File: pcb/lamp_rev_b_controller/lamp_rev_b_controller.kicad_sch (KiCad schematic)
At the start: 155 parts, among them J1 TYPE-C 3.1 MT 16P, J10 2-pin NTC header, J11 2-pin NTC header, J12 DB128H-5.08-2P-BK-S, J13 DB128H-5.08-2P-BK-S, J15 DB128H-5.08-2P-BK-S, J16 LED NTC/ID header, J17 External camera sync header, J18 SPI/FIFO camera module header, J19 Lid/cartridge/cutoff interloc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, J2 DB128H-5.08-2P-BK-S, J20 Fan PWM/tach header, J21 2x3 UART/programming header, J22 I2C expansion header, J23 Analog optical diagnostic hea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, J24 DB128H-5.08-2P high-current h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, J4 2-pin NTC header, J5 2-pin NTC header, J6 2-pin NTC header, J7 2-pin NTC header, J8 2-pin NTC header, J9 2-pin NTC header, Q1 IRLB3813PBF TO-220 12V protot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, Q2 IRLB3813PBF TO-220 12V protot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, U1 ESP32-S3-WROOM-1-N16, U10 INA180A1IDBVR gain 20 LED cur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, U2 USBLC6-2SC6, U3 Diodes AP63203WU-7 fixed 3.3V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, U4 ADS1115IDGSR, U5 CD74HC4051M, U6 TC4427ACOA/TC4427EPA, U7 CUI/Bel P7805-2000-S 5V 2A 8-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, U8 Mean Well LDD-700H 700mA CC b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, U9 SN74LVC1G08DBVR LED_EXC_PWM A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

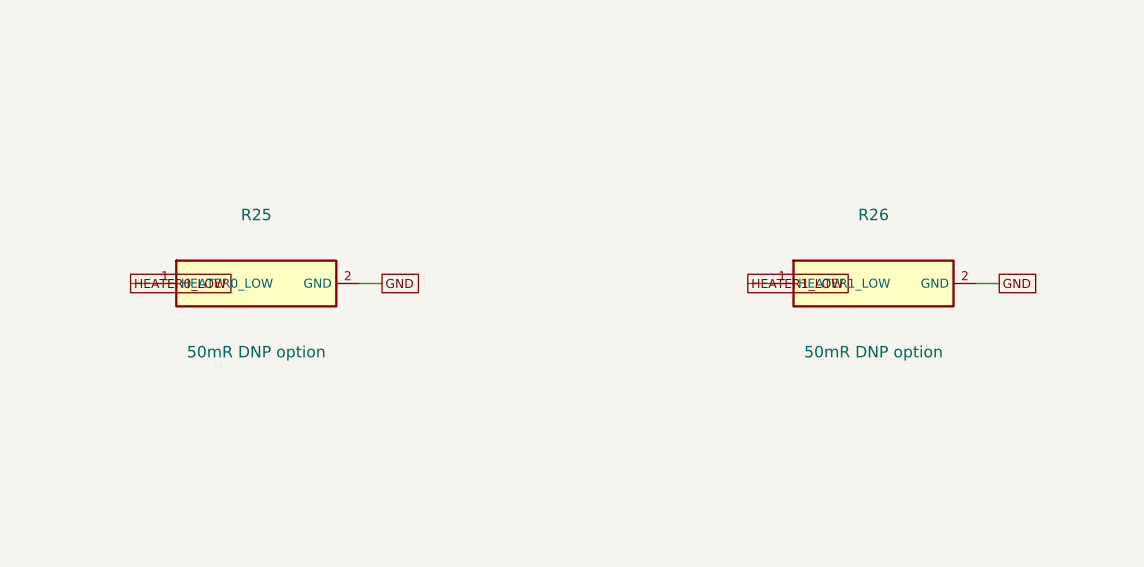
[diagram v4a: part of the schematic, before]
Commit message: Reconcile Rev B BOM and CPL fabrication classes
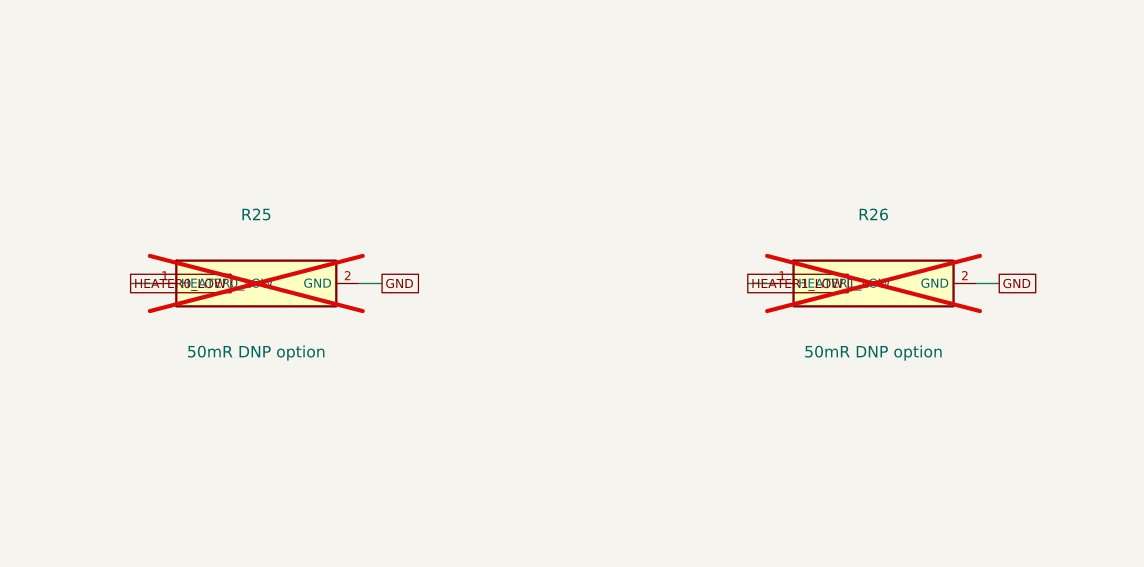
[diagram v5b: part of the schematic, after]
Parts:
- R25, R26: now not fitted
- TP_3V3, TP_3V3A, TP_5V, TP_ADS_AIN0, TP_ADS_AIN1, TP_ADS_AIN2, TP_ADS_AIN3, TP_AUX_ANALOG, TP_BOOT, TP_CAM_CS, TP_CAM_FRAME, TP_CAM_PWDN, TP_CAM_RESET, TP_CART, TP_CUTOFF, TP_EN, TP_EXPOSURE, TP_FAN_PWM, TP_FAN_TACH, TP_FAULT, TP_FRAME_TRIG, TP_GND, TP_HEATER0_GATE, TP_HEATER0_LOW, TP_HEATER0_PWM, TP_HEATER1_GATE, TP_HEATER1_LOW, TP_HEATER1_PWM, TP_HEATER_ARM, TP_HEATER_SENSE, TP_I2C_SCL, TP_I2C_SDA, TP_LATCH, TP_LED_EN, TP_LED_PWM, TP_LED_SENSE, TP_LED_SUPPLY, TP_LED_SYNC, TP_LID, TP_RUN, TP_SD_CS, TP_SPARE42, TP_SPI_MISO, TP_SPI_MOSI, TP_SPI_SCLK, TP_THERM_EN, TP_THERM_OUT, TP_THERM_S0, TP_THERM_S1, TP_THERM_S2, TP_UART_RX, TP_UART_TX, TP_USB_CC1, TP_USB_CC2, TP_USB_DN, TP_USB_DP, TP_VBUS, TP_VDRV, TP_VIN, TP_VIN_HEATER, TP_VIN_PROT: LCSC Part DNP_TESTPOINT -> VIRTUAL_TESTPOINT; Notes Schematic capture test point generated from placement.toml -> Virtual PCB test pad generated from placement.toml; exclude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; now left out of the parts list

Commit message: Resolve Rev B controller U1 exposed pad grounding
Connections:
- net GND_EP is gone; now on net GND: U1.41 (GND)
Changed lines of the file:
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@@
     (stroke (width 0) (type default))
   )
-  (global_label "GND_EP" (shape passive)
+  (global_label "GND" (shape passive)
     (at 113.03 746.76 0)
     (effects (font (size 1.0 1.0)) (justify left))

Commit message: Complete Rev B analog front end reconciliation
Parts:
- removed U10: INA180A1IDBVR gain 20 LED current sense, lcsc:SOT-23-5, symbol LF_CAPTURE_U10
- removed U9: SN74LVC1G08DBVR LED_EXC_PWM AND LED_EXC_EN, lcsc:SOT-23-5, symbol LF_CAPTURE_U9
- J23: Notes Analog optical diagnostic header. -> Analog optical diagnostic header. Pins 3 and 4 are the same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
- R25: value 50mR DNP option -> 50mR DNP forbidden low-side bypass placeholder; Notes HEATER0 optional current shunt. -> DNP forbidden bypass placeholder. Populating R25 directly b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
- R26: value 50mR DNP option -> 50mR DNP forbidden low-side bypass placeholder; Notes HEATER1 optional current shunt. -> DNP forbidden bypass placeholder. Populating R26 directly b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
- TP_ADS_AIN0: value test point ADS_AIN0 -> test point THERM_MUX_OUT
- TP_ADS_AIN2: renamed from TP_ADS_AIN1; value test point ADS_AIN1 -> test point LED_CURRENT_SENSE; symbol LF_CAPTURE_TP_ADS_AIN1 -> LF_CAPTURE_TP_ADS_AIN2
- TP_ADS_AIN3: renamed from TP_ADS_AIN2; value test point ADS_AIN2 -> test point AUX_ANALOG_IN; symbol LF_CAPTURE_TP_ADS_AIN2 -> LF_CAPTURE_TP_ADS_AIN3
- TP_AUX_ANALOG: renamed from TP_ADS_AIN3; value test point ADS_AIN3 -> test point AUX_ANALOG_IN; symbol LF_CAPTURE_TP_ADS_AIN3 -> LF_CAPTURE_TP_AUX_ANALOG
- TP_BOOT: renamed from TP_AUX_ANALOG; value test point AUX_ANALOG_IN -> test point ESP_GPIO0_BOOT; symbol LF_CAPTURE_TP_AUX_ANALOG -> LF_CAPTURE_TP_BOOT
- TP_CAM_CS: renamed from TP_BOOT; value test point ESP_GPIO0_BOOT -> test point CAM_CS_N; symbol LF_CAPTURE_TP_BOOT -> LF_CAPTURE_TP_CAM_CS
- TP_CAM_FRAME: renamed from TP_CAM_CS; value test point CAM_CS_N -> test point CAM_FRAME_INT; symbol LF_CAPTURE_TP_CAM_CS -> LF_CAPTURE_TP_CAM_FRAME
- TP_CAM_PWDN: renamed from TP_CAM_FRAME; value test point CAM_FRAME_INT -> test point CAM_PWDN_N; symbol LF_CAPTURE_TP_CAM_FRAME -> LF_CAPTURE_TP_CAM_PWDN
- TP_CAM_RESET: renamed from TP_CAM_PWDN; value test point CAM_PWDN_N -> test point CAM_RESET_N; symbol LF_CAPTURE_TP_CAM_PWDN -> LF_CAPTURE_TP_CAM_RESET
- TP_CART: renamed from TP_CAM_RESET; value test point CAM_RESET_N -> test point CART_PRESENT_N; symbol LF_CAPTURE_TP_CAM_RESET -> LF_CAPTURE_TP_CART
- TP_CUTOFF: renamed from TP_CART; value test point CART_PRESENT_N -> test point AUX_IO0_THERMAL_CUTOFF_OK; symbol LF_CAPTURE_TP_CART -> LF_CAPTURE_TP_CUTOFF
- TP_EN: renamed from TP_CUTOFF; value test point AUX_IO0_THERMAL_CUTOFF_OK -> test point ESP_EN; symbol LF_CAPTURE_TP_CUTOFF -> LF_CAPTURE_TP_EN
- TP_EXPOSURE: renamed from TP_EN; value test point ESP_EN -> test point EXPOSURE_ACTIVE_IN; symbol LF_CAPTURE_TP_EN -> LF_CAPTURE_TP_EXPOSURE
- TP_FAN_PWM: renamed from TP_EXPOSURE; value test point EXPOSURE_ACTIVE_IN -> test point FAN_PWM; symbol LF_CAPTURE_TP_EXPOSURE -> LF_CAPTURE_TP_FAN_PWM
- TP_FAN_TACH: renamed from TP_FAN_PWM; value test point FAN_PWM -> test point FAN_TACH; symbol LF_CAPTURE_TP_FAN_PWM -> LF_CAPTURE_TP_FAN_TACH
- TP_FAULT: renamed from TP_FAN_TACH; value test point FAN_TACH -> test point STATUS_FAULT_LED; symbol LF_CAPTURE_TP_FAN_TACH -> LF_CAPTURE_TP_FAULT
- TP_FRAME_TRIG: renamed from TP_FAULT; value test point STATUS_FAULT_LED -> test point FRAME_TRIG_OUT; symbol LF_CAPTURE_TP_FAULT -> LF_CAPTURE_TP_FRAME_TRIG
- TP_GND: renamed from TP_FRAME_TRIG; value test point FRAME_TRIG_OUT -> test point GND; symbol LF_CAPTURE_TP_FRAME_TRIG -> LF_CAPTURE_TP_GND
- TP_HEATER0_GATE: renamed from TP_GND; value test point GND -> test point HEATER0_GATE; symbol LF_CAPTURE_TP_GND -> LF_CAPTURE_TP_HEATER0_GATE
- TP_HEATER0_LOW: renamed from TP_HEATER0_GATE; value test point HEATER0_GATE -> test point HEATER0_LOW; symbol LF_CAPTURE_TP_HEATER0_GATE -> LF_CAPTURE_TP_HEATER0_LOW
- TP_HEATER0_PWM: renamed from TP_HEATER0_LOW; value test point HEATER0_LOW -> test point HEATER0_PWM; symbol LF_CAPTURE_TP_HEATER0_LOW -> LF_CAPTURE_TP_HEATER0_PWM
- TP_HEATER1_GATE: renamed from TP_HEATER0_PWM; value test point HEATER0_PWM -> test point HEATER1_GATE; symbol LF_CAPTURE_TP_HEATER0_PWM -> LF_CAPTURE_TP_HEATER1_GATE
- TP_HEATER1_LOW: renamed from TP_HEATER1_GATE; value test point HEATER1_GATE -> test point HEATER1_LOW; symbol LF_CAPTURE_TP_HEATER1_GATE -> LF_CAPTURE_TP_HEATER1_LOW
- TP_HEATER1_PWM: renamed from TP_HEATER1_LOW; value test point HEATER1_LOW -> test point HEATER1_PWM; symbol LF_CAPTURE_TP_HEATER1_LOW -> LF_CAPTURE_TP_HEATER1_PWM
- TP_HEATER_ARM: renamed from TP_HEATER1_PWM; value test point HEATER1_PWM -> test point HEATER_ARM; symbol LF_CAPTURE_TP_HEATER1_PWM -> LF_CAPTURE_TP_HEATER_ARM
- TP_I2C_SCL: renamed from TP_HEATER_ARM; value test point HEATER_ARM -> test point I2C_SCL; symbol LF_CAPTURE_TP_HEATER_ARM -> LF_CAPTURE_TP_I2C_SCL
- TP_I2C_SDA: renamed from TP_HEATER_SENSE; value test point HEATER_SUPPLY_SENSE -> test point I2C_SDA; symbol LF_CAPTURE_TP_HEATER_SENSE -> LF_CAPTURE_TP_I2C_SDA
- TP_LATCH: renamed from TP_I2C_SCL; value test point I2C_SCL -> test point LATCH_LOCKED_N; symbol LF_CAPTURE_TP_I2C_SCL -> LF_CAPTURE_TP_LATCH
- TP_LED_EN: renamed from TP_I2C_SDA; value test point I2C_SDA -> test point LED_EXC_EN; symbol LF_CAPTURE_TP_I2C_SDA -> LF_CAPTURE_TP_LED_EN
- TP_LED_PWM: renamed from TP_LATCH; value test point LATCH_LOCKED_N -> test point LED_EXC_PWM; symbol LF_CAPTURE_TP_LATCH -> LF_CAPTURE_TP_LED_PWM
- TP_LED_SENSE: renamed from TP_LED_EN; value test point LED_EXC_EN -> test point LED_CURRENT_SENSE; symbol LF_CAPTURE_TP_LED_EN -> LF_CAPTURE_TP_LED_SENSE
- TP_LED_SUPPLY: renamed from TP_LED_PWM; value test point LED_EXC_PWM -> test point LED_SUPPLY; symbol LF_CAPTURE_TP_LED_PWM -> LF_CAPTURE_TP_LED_SUPPLY
- TP_LED_SYNC: renamed from TP_LED_SENSE; value test point LED_CURRENT_SENSE -> test point LED_SYNC_OUT; symbol LF_CAPTURE_TP_LED_SENSE -> LF_CAPTURE_TP_LED_SYNC
- TP_LID: renamed from TP_LED_SUPPLY; value test point LED_SUPPLY -> test point LID_CLOSED_N; symbol LF_CAPTURE_TP_LED_SUPPLY -> LF_CAPTURE_TP_LID
- TP_RUN: renamed from TP_LED_SYNC; value test point LED_SYNC_OUT -> test point STATUS_RUN_LED; symbol LF_CAPTURE_TP_LED_SYNC -> LF_CAPTURE_TP_RUN
- TP_SD_CS: renamed from TP_LID; value test point LID_CLOSED_N -> test point SD_CS_N; symbol LF_CAPTURE_TP_LID -> LF_CAPTURE_TP_SD_CS
- TP_SPARE42: renamed from TP_RUN; value test point STATUS_RUN_LED -> test point SPARE_GPIO42; symbol LF_CAPTURE_TP_RUN -> LF_CAPTURE_TP_SPARE42
- TP_SPI_MISO: renamed from TP_SD_CS; value test point SD_CS_N -> test point SPI_MISO; symbol LF_CAPTURE_TP_SD_CS -> LF_CAPTURE_TP_SPI_MISO
- TP_SPI_MOSI: renamed from TP_SPARE42; value test point SPARE_GPIO42 -> test point SPI_MOSI; symbol LF_CAPTURE_TP_SPARE42 -> LF_CAPTURE_TP_SPI_MOSI
- TP_SPI_SCLK: renamed from TP_SPI_MISO; value test point SPI_MISO -> test point SPI_SCLK; symbol LF_CAPTURE_TP_SPI_MISO -> LF_CAPTURE_TP_SPI_SCLK
- TP_THERM_EN: renamed from TP_SPI_MOSI; value test point SPI_MOSI -> test point THERM_MUX_EN_N; symbol LF_CAPTURE_TP_SPI_MOSI -> LF_CAPTURE_TP_THERM_EN
- TP_THERM_OUT: renamed from TP_SPI_SCLK; value test point SPI_SCLK -> test point THERM_MUX_OUT; symbol LF_CAPTURE_TP_SPI_SCLK -> LF_CAPTURE_TP_THERM_OUT
- TP_THERM_S0: renamed from TP_THERM_EN; value test point THERM_MUX_EN_N -> test point THERM_MUX_S0; symbol LF_CAPTURE_TP_THERM_EN -> LF_CAPTURE_TP_THERM_S0
- TP_THERM_S1: renamed from TP_THERM_OUT; value test point THERM_MUX_OUT -> test point THERM_MUX_S1; symbol LF_CAPTURE_TP_THERM_OUT -> LF_CAPTURE_TP_THERM_S1
- TP_THERM_S2: renamed from TP_THERM_S0; value test point THERM_MUX_S0 -> test point THERM_MUX_S2; symbol LF_CAPTURE_TP_THERM_S0 -> LF_CAPTURE_TP_THERM_S2
- TP_UART_RX: renamed from TP_THERM_S1; value test point THERM_MUX_S1 -> test point UART0_RXD; symbol LF_CAPTURE_TP_THERM_S1 -> LF_CAPTURE_TP_UART_RX
- TP_UART_TX: renamed from TP_THERM_S2; value test point THERM_MUX_S2 -> test point UART0_TXD; symbol LF_CAPTURE_TP_THERM_S2 -> LF_CAPTURE_TP_UART_TX
- TP_USB_CC1: renamed from TP_UART_RX; value test point UART0_RXD -> test point USB_CC1; symbol LF_CAPTURE_TP_UART_RX -> LF_CAPTURE_TP_USB_CC1
- TP_USB_CC2: renamed from TP_UART_TX; value test point UART0_TXD -> test point USB_CC2; symbol LF_CAPTURE_TP_UART_TX -> LF_CAPTURE_TP_USB_CC2
- TP_USB_DN: renamed from TP_USB_CC1; value test point USB_CC1 -> test point USB_DN; symbol LF_CAPTURE_TP_USB_CC1 -> LF_CAPTURE_TP_USB_DN
- TP_USB_DP: renamed from TP_USB_CC2; value test point USB_CC2 -> test point USB_DP; symbol LF_CAPTURE_TP_USB_CC2 -> LF_CAPTURE_TP_USB_DP
- TP_VBUS: renamed from TP_USB_DN; value test point USB_DN -> test point VBUS; symbol LF_CAPTURE_TP_USB_DN -> LF_CAPTURE_TP_VBUS
- TP_VDRV: renamed from TP_USB_DP; value test point USB_DP -> test point VDRV; symbol LF_CAPTURE_TP_USB_DP -> LF_CAPTURE_TP_VDRV
- TP_VIN: renamed from TP_VBUS; value test point VBUS -> test point VIN_12_24; symbol LF_CAPTURE_TP_VBUS -> LF_CAPTURE_TP_VIN
- TP_VIN_HEATER: renamed from TP_VDRV; value test point VDRV -> test point VIN_HEATER; symbol LF_CAPTURE_TP_VDRV -> LF_CAPTURE_TP_VIN_HEATER
- TP_VIN_PROT: renamed from TP_VIN; value test point VIN_12_24 -> test point VIN_PROTECTED; symbol LF_CAPTURE_TP_VIN -> LF_CAPTURE_TP_VIN_PROT
- U1: renamed from TP_VIN_HEATER; value test point VIN_HEATER -> ESP32-S3-WROOM-1-N16; footprint lcsc:TESTPOINT_SMD_1.5MM -> lcsc:WIFIM-SMD_ESP32-S3-WROOM-1-N8; symbol LF_CAPTURE_TP_VIN_HEATER -> LF_CAPTURE_U1; LCSC Part VIRTUAL_TESTPOINT -> DigiKey 1965-ESP32-S3-WROOM-1-N16-ND; Notes Virtual PCB test pad generated from placement.toml; exclude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 -> ESP32-S3-WROOM-1-N16 using verified-compatible N8 land patt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; now in the parts list
- U10: renamed from U8; value Mean Well LDD-700H 700mA CC buck LED driver; LDD-1000H C17529736 DNP thermal-validation alternate -> INA180A1IDBVR gain 20 LED current sense; footprint lcsc:MEANWELL_LDD-300-1000H_THT -> lcsc:SOT-23-5; symbol LF_CAPTURE_U8 -> LF_CAPTURE_U10; LCSC Part C17537709 -> C122228; Notes Mean Well LDD-700H LED driver module. LDD-H -Vin/GND and -V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 -> INA180A1IDBVR LED current telemetry across high-side output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
- U2: renamed from TP_VIN_PROT; value test point VIN_PROTECTED -> USBLC6-2SC6; footprint lcsc:TESTPOINT_SMD_1.5MM -> lcsc:SOT-23-6; symbol LF_CAPTURE_TP_VIN_PROT -> LF_CAPTURE_U2; LCSC Part VIRTUAL_TESTPOINT -> C7519; Notes Virtual PCB test pad generated from placement.toml; exclude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 -> USB data ESD protection.; now in the parts list
- U3: renamed from U1; value ESP32-S3-WROOM-1-N16 -> Diodes AP63203WU-7 fixed 3.3V 2A buck; footprint lcsc:WIFIM-SMD_ESP32-S3-WROOM-1-N8 -> lcsc:TSOT26_AP63203WU; symbol LF_CAPTURE_U1 -> LF_CAPTURE_U3; LCSC Part DigiKey 1965-ESP32-S3-WROOM-1-N16-ND -> C780769; Notes ESP32-S3-WROOM-1-N16 using verified-compatible N8 land patt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 -> Diodes AP63203WU-7 fixed 3.3 V buck regulator.
- U4: renamed from U2; value USBLC6-2SC6 -> ADS1115IDGSR; footprint lcsc:SOT-23-6 -> lcsc:MSOP-10_L3.0-W3.0-P0.50-LS5.0-BL; symbol LF_CAPTURE_U2 -> LF_CAPTURE_U4; LCSC Part C7519 -> C37593; Notes USB data ESD protection. -> ADS1115 direct single-ended front end: AIN0 receives the fi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
- U5: renamed from U3; value Diodes AP63203WU-7 fixed 3.3V 2A buck -> CD74HC4051M; footprint lcsc:TSOT26_AP63203WU -> lcsc:SOIC-16_L9.9-W3.9-P1.27-LS6.0-BL; symbol LF_CAPTURE_U3 -> LF_CAPTURE_U5; LCSC Part C780769 -> C139301; Notes Diodes AP63203WU-7 fixed 3.3 V buck regulator. -> CD74HC4051 thermistor mux.
- U6: renamed from U4; value ADS1115IDGSR -> TC4427ACOA/TC4427EPA; footprint lcsc:MSOP-10_L3.0-W3.0-P0.50-LS5.0-BL -> lcsc:SOIC-8_L4.9-W3.9-P1.27-LS6.0-BL; symbol LF_CAPTURE_U4 -> LF_CAPTURE_U6; LCSC Part C37593 -> DigiKey TC4427EPA-ND or C636886 SMD alternate; Notes ADS1115 thermal/slow analog ADC. -> TC4427 dual heater gate-driver interface.
- U7: renamed from U5; value CD74HC4051M -> CUI/Bel P7805-2000-S 5V 2A 8-36V buck module; hand-place no-substitution; footprint lcsc:SOIC-16_L9.9-W3.9-P1.27-LS6.0-BL -> lcsc:P78-2000-S_SIP3; symbol LF_CAPTURE_U5 -> LF_CAPTURE_U7; LCSC Part C139301 -> C2848816; Notes CD74HC4051 thermistor mux. -> CUI/Bel P7805-2000-S 5 V / 2 A buck module.
- U8: renamed from U6; value TC4427ACOA/TC4427EPA -> Mean Well LDD-700H 700mA CC buck LED driver; LDD-1000H C17529736 DNP thermal-validation alternate; footprint lcsc:SOIC-8_L4.9-W3.9-P1.27-LS6.0-BL -> lcsc:MEANWELL_LDD-300-1000H_THT; symbol LF_CAPTURE_U6 -> LF_CAPTURE_U8; LCSC Part DigiKey TC4427EPA-ND or C636886 SMD alternate -> C17537709; Notes TC4427 dual heater gate-driver interface. -> Mean Well LDD-700H LED driver module. LDD-H -Vin/GND and -V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
- U9: renamed from U7; value CUI/Bel P7805-2000-S 5V 2A 8-36V buck module; hand-place no-substitution -> SN74LVC1G08DBVR LED_EXC_PWM AND LED_EXC_EN; footprint lcsc:P78-2000-S_SIP3 -> lcsc:SOT-23-5; symbol LF_CAPTURE_U7 -> LF_CAPTURE_U9; LCSC Part C2848816 -> C7666; Notes CUI/Bel P7805-2000-S 5 V / 2 A buck module. -> SN74LVC1G08DBVR gates LED_EXC_PWM and LED_EXC_EN.
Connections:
- net HEATER_SUPPLY_SENSE is gone; now on net I2C_SDA: TP_I2C_SDA.1 (I2C_SDA)
- net +3V3: now also U1.2 (+3V3), U10.5 (+3V3), U3.1 (+3V3), U4.8 (+3V3), U9.5 (+3V3); no longer U3.2 (+3V3), U5.1 (+3V3), U6.8 (+3V3)
- net +3V3_ANA: now also U5.16 (+3V3_ANA); no longer U7.16 (+3V3_ANA)
- net +5V: now also U3.2 (+5V), U3.4 (+5V), U7.3 (+5V); no longer U5.2 (+5V), U5.4 (+5V), U9.3 (+5V)
- net 3V3_BST: now also U3.6 (3V3_BST); no longer U5.6 (3V3_BST)
- net 3V3_SW: now also U3.5 (3V3_SW); no longer U5.5 (3V3_SW)
- net AUX_ANALOG_IN: now also J23.3 (AUX_ANALOG_IN), TP_ADS_AIN3.1 (AUX_ANALOG_IN), TP_AUX_ANALOG.1 (AUX_ANALOG_IN), U4.7 (AUX_ANALOG_IN); no longer TP_BOOT.1 (AUX_ANALOG_IN)
- net AUX_IO0_THERMAL_CUTOFF_OK: now also TP_CUTOFF.1 (AUX_IO0_THERMAL_CUTOFF_OK), U1.32 (AUX_IO0_THERMAL_CUTOFF_OK); no longer TP_EN.1 (AUX_IO0_THERMAL_CUTOFF_OK), U3.32 (AUX_IO0_THERMAL_CUTOFF_OK)
- net CAM_CS_N: now also TP_CAM_CS.1 (CAM_CS_N), U1.20 (CAM_CS_N); no longer TP_CAM_FRAME.1 (CAM_CS_N), U3.20 (CAM_CS_N)
- net CAM_FRAME_INT: now also TP_CAM_FRAME.1 (CAM_FRAME_INT), U1.21 (CAM_FRAME_INT); no longer TP_CAM_PWDN.1 (CAM_FRAME_INT), U3.21 (CAM_FRAME_INT)
- net CAM_PWDN_N: now also TP_CAM_PWDN.1 (CAM_PWDN_N), U1.22 (CAM_PWDN_N); no longer TP_CAM_RESET.1 (CAM_PWDN_N), U3.22 (CAM_PWDN_N)
- net CAM_RESET_N: now also TP_CAM_RESET.1 (CAM_RESET_N), U1.8 (CAM_RESET_N); no longer TP_CART.1 (CAM_RESET_N), U3.8 (CAM_RESET_N)
- net CART_PRESENT_N: now also TP_CART.1 (CART_PRESENT_N), U1.31 (CART_PRESENT_N); no longer TP_CUTOFF.1 (CART_PRESENT_N), U3.31 (CART_PRESENT_N)
- net ESP_EN: now also TP_EN.1 (ESP_EN), U1.3 (ESP_EN); no longer TP_EXPOSURE.1 (ESP_EN), U3.3 (ESP_EN)
- net ESP_GPIO0_BOOT: now also TP_BOOT.1 (ESP_GPIO0_BOOT), U1.27 (ESP_GPIO0_BOOT); no longer TP_CAM_CS.1 (ESP_GPIO0_BOOT), U3.27 (ESP_GPIO0_BOOT)
- net EXPOSURE_ACTIVE_IN: now also TP_EXPOSURE.1 (EXPOSURE_ACTIVE_IN), U1.29 (EXPOSURE_ACTIVE_IN); no longer TP_FAN_PWM.1 (EXPOSURE_ACTIVE_IN), U3.29 (EXPOSURE_ACTIVE_IN)
- net FAN_PWM: now also TP_FAN_PWM.1 (FAN_PWM); no longer TP_FAN_TACH.1 (FAN_PWM)
- net FAN_TACH: now also TP_FAN_TACH.1 (FAN_TACH); no longer TP_FAULT.1 (FAN_TACH)
- net FRAME_TRIG_OUT: now also TP_FRAME_TRIG.1 (FRAME_TRIG_OUT), U1.25 (FRAME_TRIG_OUT); no longer TP_GND.1 (FRAME_TRIG_OUT), U3.25 (FRAME_TRIG_OUT)
- net GND: now also TP_GND.1 (GND), U1.1 (GND), U1.40 (GND), U1.41 (GND), U2.2 (GND), U3.3 (GND), U4.1 (GND), U4.3 (GND), U5.7 (GND), U5.8 (GND), U6.4 (GND), U7.2 (GND), U8.1 (GND), U8.2 (GND); no longer TP_HEATER0_GATE.1 (GND), U10.1 (GND), U3.1 (GND), U3.40 (GND), U3.41 (GND), U4.2 (GND), U5.3 (GND), U6.1 (GND), U7.7 (GND), U7.8 (GND), U8.3 (GND), U8.4 (GND)
- net HEATER0_GATE: now also TP_HEATER0_GATE.1 (HEATER0_GATE), U6.7 (HEATER0_GATE); no longer TP_HEATER0_LOW.1 (HEATER0_GATE), U8.7 (HEATER0_GATE)
- net HEATER0_LOW: now also TP_HEATER0_LOW.1 (HEATER0_LOW); no longer TP_HEATER0_PWM.1 (HEATER0_LOW)
- net HEATER0_PWM: now also TP_HEATER0_PWM.1 (HEATER0_PWM), U1.10 (HEATER0_PWM), U6.2 (HEATER0_PWM); no longer TP_HEATER1_GATE.1 (HEATER0_PWM), U3.10 (HEATER0_PWM), U8.2 (HEATER0_PWM)
- net HEATER1_GATE: now also TP_HEATER1_GATE.1 (HEATER1_GATE), U6.5 (HEATER1_GATE); no longer TP_HEATER1_LOW.1 (HEATER1_GATE), U8.5 (HEATER1_GATE)
- net HEATER1_LOW: now also TP_HEATER1_LOW.1 (HEATER1_LOW); no longer TP_HEATER1_PWM.1 (HEATER1_LOW)
- net HEATER1_PWM: now also TP_HEATER1_PWM.1 (HEATER1_PWM), U1.11 (HEATER1_PWM), U6.8 (HEATER1_PWM); no longer TP_HEATER_ARM.1 (HEATER1_PWM), U3.11 (HEATER1_PWM), U8.8 (HEATER1_PWM)
- net HEATER_ARM: now also TP_HEATER_ARM.1 (HEATER_ARM), U1.9 (HEATER_ARM), U6.1 (HEATER_ARM); no longer TP_I2C_SCL.1 (HEATER_ARM), U3.9 (HEATER_ARM), U8.1 (HEATER_ARM)
- net I2C_SCL: now also TP_I2C_SCL.1 (I2C_SCL), U1.38 (I2C_SCL), U4.10 (I2C_SCL); no longer TP_LATCH.1 (I2C_SCL), U3.38 (I2C_SCL), U6.10 (I2C_SCL)
- net I2C_SDA: now also U1.39 (I2C_SDA), U4.9 (I2C_SDA); no longer TP_LED_EN.1 (I2C_SDA), U3.39 (I2C_SDA), U6.9 (I2C_SDA)
- net LATCH_LOCKED_N: now also TP_LATCH.1 (LATCH_LOCKED_N); no longer TP_LED_PWM.1 (LATCH_LOCKED_N)
- net LED_CURRENT_SENSE: now also TP_ADS_AIN2.1 (LED_CURRENT_SENSE), TP_LED_SENSE.1 (LED_CURRENT_SENSE), U10.4 (LED_CURRENT_SENSE), U4.6 (LED_CURRENT_SENSE); no longer TP_LED_SYNC.1 (LED_CURRENT_SENSE)
- net LED_DIM_DRIVE: now also U8.22 (LED_DIM_DRIVE); no longer U10.22 (LED_DIM_DRIVE)
- net LED_DIM_GATE: now also U9.4 (LED_DIM_GATE)
- net LED_DRV_PLUS: now also U10.1 (LED_DRV_PLUS), U8.13 (LED_DRV_PLUS), U8.14 (LED_DRV_PLUS); no longer U10.13 (LED_DRV_PLUS), U10.14 (LED_DRV_PLUS)
- net LED_EXC_EN: now also TP_LED_EN.1 (LED_EXC_EN), U1.24 (LED_EXC_EN), U9.3 (LED_EXC_EN); no longer TP_LED_SENSE.1 (LED_EXC_EN), U3.24 (LED_EXC_EN)
- net LED_EXC_PWM: now also TP_LED_PWM.1 (LED_EXC_PWM), U1.7 (LED_EXC_PWM), U9.1 (LED_EXC_PWM); no longer TP_LED_SUPPLY.1 (LED_EXC_PWM), U3.7 (LED_EXC_PWM)
- net LED_MINUS: now also U8.11 (LED_MINUS), U8.12 (LED_MINUS); no longer U10.11 (LED_MINUS), U10.12 (LED_MINUS)
- net LED_PLUS: now also U10.3 (LED_PLUS)
- net LED_SUPPLY: now also TP_LED_SUPPLY.1 (LED_SUPPLY), U8.23 (LED_SUPPLY), U8.24 (LED_SUPPLY); no longer TP_LID.1 (LED_SUPPLY), U10.23 (LED_SUPPLY), U10.24 (LED_SUPPLY)
- net LED_SYNC_OUT: now also TP_LED_SYNC.1 (LED_SYNC_OUT), U1.28 (LED_SYNC_OUT); no longer TP_RUN.1 (LED_SYNC_OUT), U3.28 (LED_SYNC_OUT)
- net LID_CLOSED_N: now also TP_LID.1 (LID_CLOSED_N), U1.30 (LID_CLOSED_N); no longer TP_SD_CS.1 (LID_CLOSED_N), U3.30 (LID_CLOSED_N)
- net SD_CS_N: now also TP_SD_CS.1 (SD_CS_N), U1.23 (SD_CS_N); no longer TP_SPI_MISO.1 (SD_CS_N), U3.23 (SD_CS_N)
- net SPARE_GPIO42: now also TP_SPARE42.1 (SPARE_GPIO42), U1.35 (SPARE_GPIO42); no longer TP_SPI_MOSI.1 (SPARE_GPIO42), U3.35 (SPARE_GPIO42)
- net SPI_MISO: now also TP_SPI_MISO.1 (SPI_MISO), U1.19 (SPI_MISO); no longer TP_SPI_SCLK.1 (SPI_MISO), U3.19 (SPI_MISO)
- net SPI_MOSI: now also TP_SPI_MOSI.1 (SPI_MOSI), U1.18 (SPI_MOSI); no longer TP_THERM_EN.1 (SPI_MOSI), U3.18 (SPI_MOSI)
- net SPI_SCLK: now also TP_SPI_SCLK.1 (SPI_SCLK), U1.17 (SPI_SCLK); no longer TP_THERM_OUT.1 (SPI_SCLK), U3.17 (SPI_SCLK)
- net STATUS_FAULT_LED: now also TP_FAULT.1 (STATUS_FAULT_LED), U1.34 (STATUS_FAULT_LED); no longer TP_FRAME_TRIG.1 (STATUS_FAULT_LED), U3.34 (STATUS_FAULT_LED)
- net STATUS_RUN_LED: now also TP_RUN.1 (STATUS_RUN_LED), U1.33 (STATUS_RUN_LED); no longer TP_SPARE42.1 (STATUS_RUN_LED), U3.33 (STATUS_RUN_LED)
- net THERM_CH_0: now also U5.13 (THERM_CH_0); no longer U7.13 (THERM_CH_0)
- net THERM_CH_1: now also U5.14 (THERM_CH_1); no longer U7.14 (THERM_CH_1)
- net THERM_CH_2: now also U5.15 (THERM_CH_2); no longer U7.15 (THERM_CH_2)
- net THERM_CH_3: now also U5.12 (THERM_CH_3); no longer U7.12 (THERM_CH_3)
- net THERM_CH_4: now also U5.1 (THERM_CH_4); no longer U7.1 (THERM_CH_4)
- net THERM_CH_5: now also U5.5 (THERM_CH_5); no longer U7.5 (THERM_CH_5)
- net THERM_CH_6: now also U5.2 (THERM_CH_6); no longer U7.2 (THERM_CH_6)
- net THERM_CH_7: now also U5.4 (THERM_CH_7); no longer U7.4 (THERM_CH_7)
- net THERM_MUX_EN_N: now also TP_THERM_EN.1 (THERM_MUX_EN_N), U1.12 (THERM_MUX_EN_N), U5.6 (THERM_MUX_EN_N); no longer TP_THERM_S0.1 (THERM_MUX_EN_N), U3.12 (THERM_MUX_EN_N), U7.6 (THERM_MUX_EN_N)
- net THERM_MUX_OUT: now also TP_ADS_AIN0.1 (THERM_MUX_OUT), TP_THERM_OUT.1 (THERM_MUX_OUT), U4.4 (THERM_MUX_OUT), U5.3 (THERM_MUX_OUT); no longer TP_THERM_S1.1 (THERM_MUX_OUT), U7.3 (THERM_MUX_OUT)
- net THERM_MUX_S0: now also TP_THERM_S0.1 (THERM_MUX_S0), U1.4 (THERM_MUX_S0), U5.11 (THERM_MUX_S0); no longer TP_THERM_S2.1 (THERM_MUX_S0), U3.4 (THERM_MUX_S0), U7.11 (THERM_MUX_S0)
- net THERM_MUX_S1: now also TP_THERM_S1.1 (THERM_MUX_S1), U1.5 (THERM_MUX_S1), U5.10 (THERM_MUX_S1); no longer TP_UART_RX.1 (THERM_MUX_S1), U3.5 (THERM_MUX_S1), U7.10 (THERM_MUX_S1)
- net THERM_MUX_S2: now also TP_THERM_S2.1 (THERM_MUX_S2), U1.6 (THERM_MUX_S2), U5.9 (THERM_MUX_S2); no longer TP_UART_TX.1 (THERM_MUX_S2), U3.6 (THERM_MUX_S2), U7.9 (THERM_MUX_S2)
- net UART0_RXD: now also TP_UART_RX.1 (UART0_RXD), U1.36 (UART0_RXD); no longer TP_USB_CC1.1 (UART0_RXD), U3.36 (UART0_RXD)
- net UART0_TXD: now also TP_UART_TX.1 (UART0_TXD), U1.37 (UART0_TXD); no longer TP_USB_CC2.1 (UART0_TXD), U3.37 (UART0_TXD)
- net USB_CC1: now also TP_USB_CC1.1 (USB_CC1); no longer TP_USB_DN.1 (USB_CC1)
- net USB_CC2: now also TP_USB_CC2.1 (USB_CC2); no longer TP_USB_DP.1 (USB_CC2)
- net USB_DN: now also TP_USB_DN.1 (USB_DN), U1.13 (USB_DN), U2.3 (USB_DN), U2.4 (USB_DN); no longer TP_VBUS.1 (USB_DN), U3.13 (USB_DN), U4.3 (USB_DN), U4.4 (USB_DN)
- net USB_DP: now also TP_USB_DP.1 (USB_DP), U1.14 (USB_DP), U2.1 (USB_DP), U2.6 (USB_DP); no longer TP_VDRV.1 (USB_DP), U3.14 (USB_DP), U4.1 (USB_DP), U4.6 (USB_DP)
- net VBUS: now also TP_VBUS.1 (VBUS), U2.5 (VBUS); no longer TP_VIN.1 (VBUS), U4.5 (VBUS)
- net VDRV: now also TP_VDRV.1 (VDRV), U6.6 (VDRV); no longer TP_VIN_HEATER.1 (VDRV), U8.6 (VDRV)
- net VIN_12_24: now also TP_VIN.1 (VIN_12_24); no longer TP_VIN_PROT.1 (VIN_12_24)
- net VIN_HEATER: now also TP_VIN_HEATER.1 (VIN_HEATER); no longer U1.1 (VIN_HEATER)
- net VIN_PROTECTED: now also TP_VIN_PROT.1 (VIN_PROTECTED), U7.1 (VIN_PROTECTED); no longer U2.1 (VIN_PROTECTED), U9.1 (VIN_PROTECTED)
- removed net ADS_AIN0: TP_ADS_AIN0.1 (ADS_AIN0), U6.4 (ADS_AIN0)
- removed net ADS_AIN1: TP_ADS_AIN2.1 (ADS_AIN1), U6.5 (ADS_AIN1)
- removed net ADS_AIN2: TP_ADS_AIN3.1 (ADS_AIN2), U6.6 (ADS_AIN2)
- removed net ADS_AIN3: J23.3 (ADS_AIN3), TP_AUX_ANALOG.1 (ADS_AIN3), U6.7 (ADS_AIN3)
- no-connect marks 53 -> 54
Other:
- moved on the sheet: TP_CUTOFF, TP_EN, TP_EXPOSURE, TP_FAN_PWM, TP_I2C_SDA
